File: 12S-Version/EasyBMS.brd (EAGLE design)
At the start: 49 x 100 mm, 145 parts, among them IC1 LTC6811IG-2#PBF, Q10 BSS84LT1G, Q11 BSS84LT1G, Q12 BSS84LT1G, Q13 BSS84LT1G, Q2 BSS84LT1G, Q3 BSS84LT1G, Q4 BSS84LT1G, Q5 BSS84LT1G, Q6 BSS84LT1G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

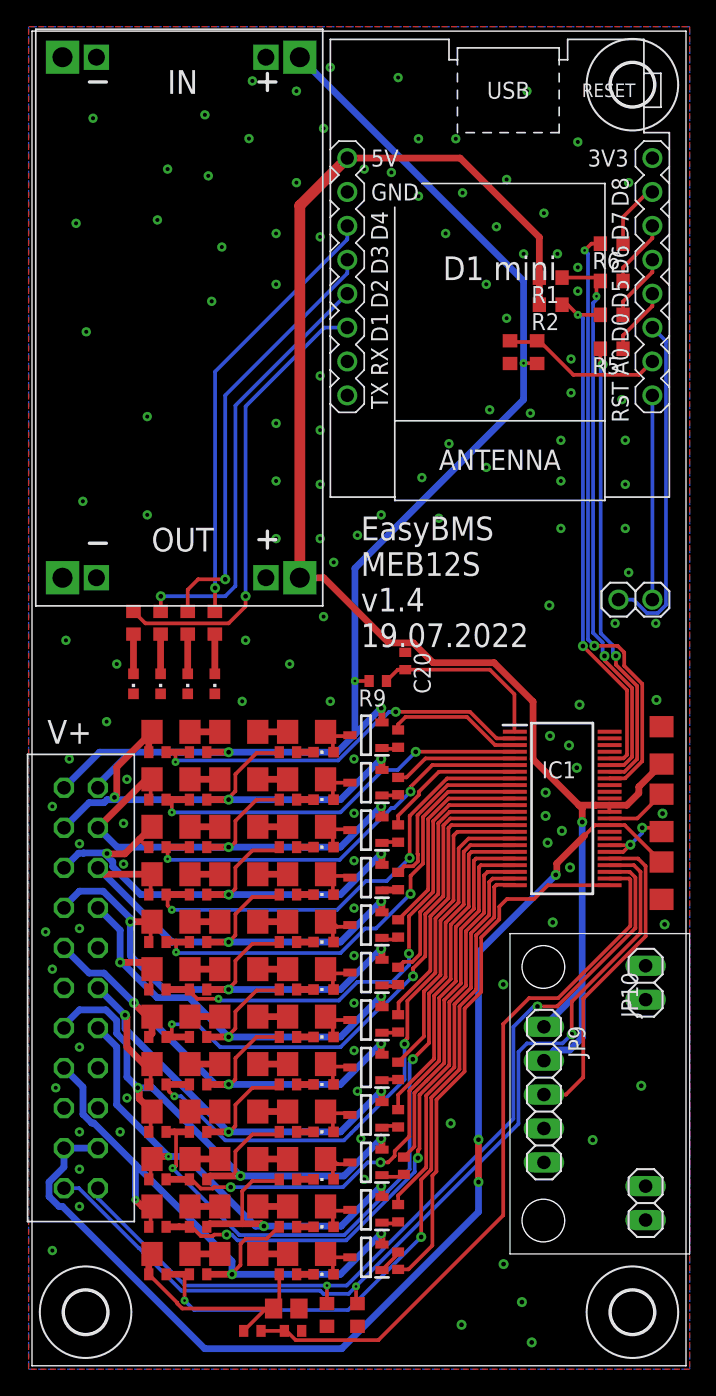
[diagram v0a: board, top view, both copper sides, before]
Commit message: Bugfix of SPI MISO pullup and Bat C1- connection
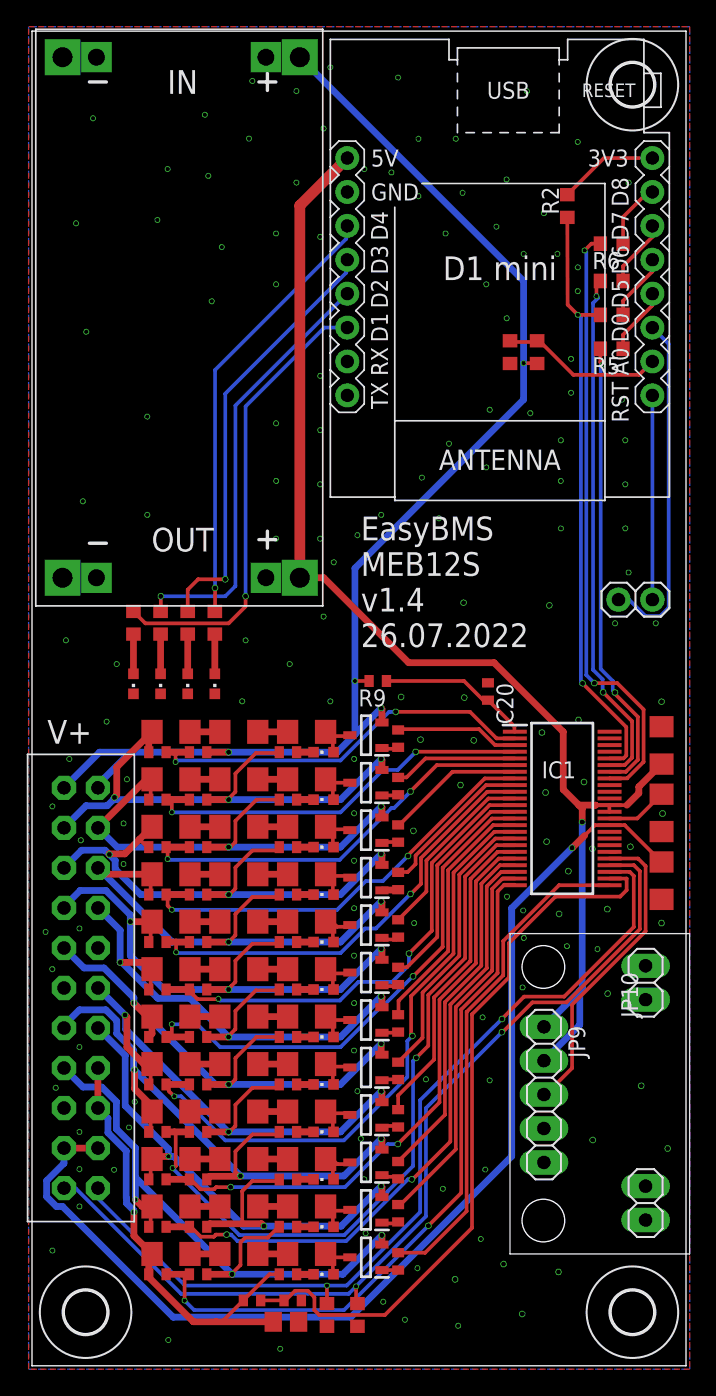
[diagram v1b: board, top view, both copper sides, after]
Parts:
- removed R1: 5K1, rcl:R0603
- moved R2 7.50 mm to (40.1, 86.9), turned to 90 degrees
- moved C20 6.61 mm to (34.2, 50.5)
- moved C5 2.29 mm to (19.5, 4.90)
- moved R3 2.29 mm to (16.5, 4.90)
- moved R13 0.99 mm to (19.0, 3.30)
- moved R34 0.54 mm to (27.4, 14.7)
- moved R10 0.05 mm to (27.4, 7.82), turned to 270 degrees
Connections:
- removed net 3V3: U$2.JP1.8
- new net +3V3: R2.2, U$2.JP1.8
- net 5VDC: no longer R1.2, R2.2
- net C1-: now also JP7.15_TOTAL-, JP7.17_TOTAL-
- net GND: no longer JP7.15_TOTAL-, JP7.17_TOTAL-
- net MOSI: no longer R1.1
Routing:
- net 5VDC: track 122.5 -> 97.4 mm
- net C1-: track 17.7 -> 34.1 mm, vias 0 -> 1
- net +3V3: track 0.00 -> 7.51 mm
- net MISO: track 39.2 -> 45.2 mm
- net GND: track 6.86 -> 1.24 mm, vias 128 -> 154
- net MOSI: track 42.1 -> 39.2 mm
- net VREF2: track 86.5 -> 83.8 mm, vias 3 -> 1
- net S1: track 39.7 -> 37.5 mm
- net V+: track 13.5 -> 11.4 mm
- net S6: track 20.6 -> 18.8 mm
- net C6: track 41.5 -> 39.7 mm
- net C9: track 34.7 -> 32.9 mm
- net S7: track 18.5 -> 16.7 mm
- net C7: track 38.0 -> 36.2 mm
- net S8: track 15.6 -> 13.9 mm
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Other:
- board text added: "EasyBMS MEB12S v1.4 26.07.2022"
- board text removed: "EasyBMS MEB12S v1.4 19.07.2022"

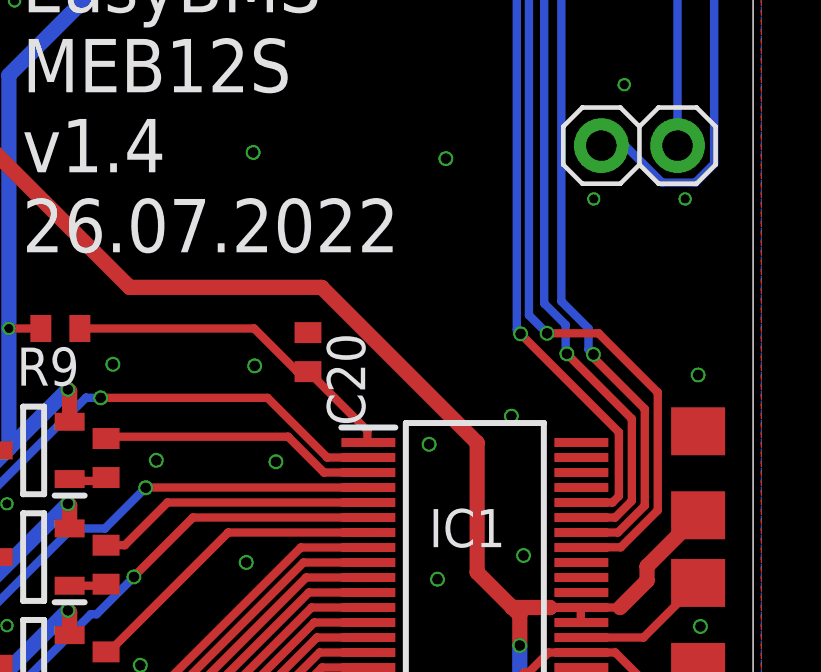
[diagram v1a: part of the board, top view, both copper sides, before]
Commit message: new branch for LTC68xx-1 chip, small changes on base board
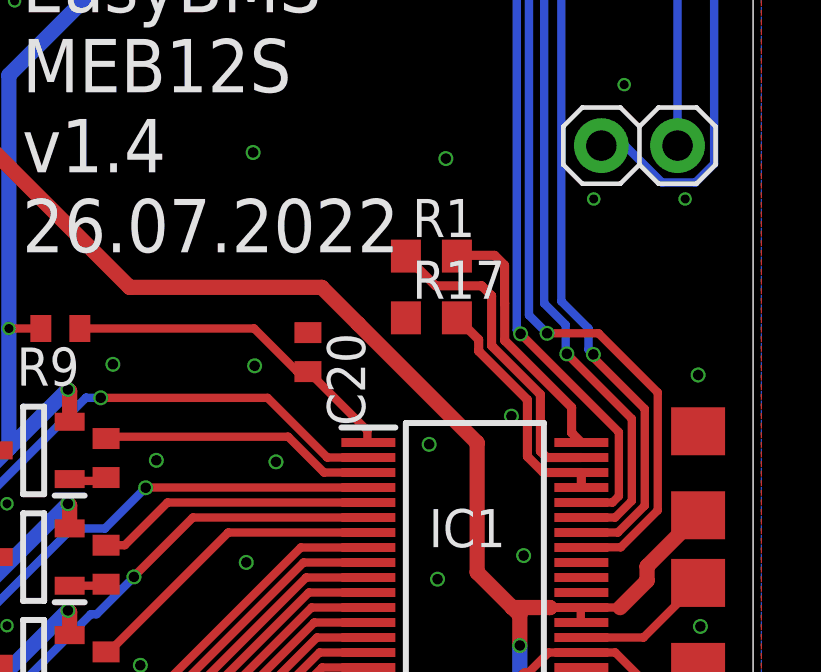
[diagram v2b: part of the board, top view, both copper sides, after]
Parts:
- added R1: 100R, rcl:R0603
- added R17: 20k, rcl:R0603
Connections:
- new net IBIAS: IC1.45, IC1.46, R17.2
- new net IMB: IC1.47, R1.1
- new net IPB: IC1.48, R1.2
- net GND: now also R17.1; no longer IC1.45, IC1.46, IC1.47, IC1.48
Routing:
- net IMB: track 0.00 -> 10.7 mm
- net IPB: track 0.00 -> 8.70 mm
- net IBIAS: track 0.00 -> 8.12 mm
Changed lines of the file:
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@@
 <drawing>
 <settings>
-<setting alwaysvectorfont="yes"/>
+<setting alwaysvectorfont="no"/>
 <setting verticaltext="up"/>
 </settings>
@@
 <attribute name="VALUE" x="18.3896" y="0.762" size="1.27" layer="27"/>
 </element>
+<element name="R1" library="rcl" library_urn="urn:adsk.eagle:library:334" package="R0603" package3d_urn="urn:adsk.eagle:package:23555/2" value="100R" x="38.2778" y="53.721" smashed="yes">
+<attribute name="NAME" x="37.6428" y="54.356" size="1.27" layer="25"/>
+<attribute name="VALUE" x="37.6428" y="51.816" size="1.27" layer="27"/>
+</element>
+<element name="R17" library="rcl" library_urn="urn:adsk.eagle:library:334" package="R0603" package3d_urn="urn:adsk.eagle:package:23555/2" value="20k" x="38.2778" y="51.6636" smashed="yes">
+<attribute name="NAME" x="37.6428" y="52.2986" size="1.27" layer="25"/>
+<attribute name="VALUE" x="37.6428" y="49.7586" size="1.27" layer="27"/>
+</element>
 </elements>
 <signals>
@@
 <wire x1="44.573" y1="42.0076" x2="45.466" y2="42.9006" width="0.2794" layer="1"/>
 <wire x1="28.2194" y1="52.6796" x2="34.6202" y2="52.6796" width="0.508" layer="1"/>
-<wire x1="34.6202" y1="52.6796" x2="39.8018" y2="47.498" width="0.508" layer="1"/>
+<wire x1="34.6202" y1="52.6796" x2="35.8394" y2="51.4604" width="0.508" layer="1"/>
+<wire x1="35.8394" y1="51.4604" x2="39.8018" y2="47.498" width="0.508" layer="1"/>
 <wire x1="21.855" y1="59.044" x2="28.2194" y2="52.6796" width="0.508" layer="1"/>
 <wire x1="39.8018" y1="43.18" x2="39.8018" y2="47.498" width="0.508" layer="1"/>
@@
 <contactref element="IC1" pad="30"/>
 <contactref element="IC1" pad="40"/>
-<contactref element="IC1" pad="48"/>
-<contactref element="IC1" pad="47"/>
-<contactref element="IC1" pad="46"/>
-<contactref element="IC1" pad="45"/>
 <contactref element="C1" pad="2"/>
 <contactref element="C5" pad="2"/>
@@
 <via x="41.9862" y="38.735" extent="1-16" drill="0.35"/>
 <via x="6.1468" y="14.6812" extent="1-16" drill="0.3"/>
+<contactref element="R17" pad="1"/>
 </signal>
 <signal name="N$202">
@@
 <wire x1="42.8502" y1="90.487" x2="46.482" y2="90.487" width="0.2794" layer="1"/>
 </signal>
+<signal name="IPB">
+<contactref element="IC1" pad="48"/>
+<contactref element="R1" pad="2"/>
+<wire x1="43.2756" y1="47.5076" x2="42.9514" y2="47.8318" width="0.3048" layer="1"/>
+<wire x1="40.719" y1="52.1434" x2="40.7162" y2="52.1462" width="0.3048" layer="1"/>
+<wire x1="40.719" y1="50.9104125" x2="40.719" y2="52.1434" width="0.3048" layer="1"/>
+<wire x1="42.9514" y1="48.6780125" x2="40.719" y2="50.9104125" width="0.3048" layer="1"/>
+<wire x1="40.7162" y1="52.1462" x2="40.7162" y2="53.4162" width="0.3048" layer="1"/>
+<wire x1="40.7162" y1="53.4162" x2="40.386" y2="53.7464" width="0.3048" layer="1"/>
+<wire x1="40.386" y1="53.7464" x2="39.1532" y2="53.7464" width="0.3048" layer="1"/>
+<wire x1="39.1532" y1="53.7464" x2="39.1278" y2="53.721" width="0.3048" layer="1"/>
+<wire x1="42.9514" y1="47.8318" x2="42.9514" y2="48.6780125" width="0.3048" layer="1"/>
+</signal>
+<signal name="IMB">
+<contactref element="IC1" pad="47"/>
+<contactref element="R1" pad="1"/>
+<wire x1="37.4278" y1="53.721" x2="38.4184" y2="52.7304" width="0.3048" layer="1"/>
+<wire x1="38.4184" y1="52.7304" x2="39.9542" y2="52.7304" width="0.3048" layer="1"/>
+<wire x1="39.9542" y1="52.7304" x2="40.2844" y2="52.4002" width="0.3048" layer="1"/>
+<wire x1="40.2844" y1="52.4002" x2="40.2844" y2="50.73435" width="0.3048" layer="1"/>
+<wire x1="42.121" y1="47.0076" x2="43.2756" y2="47.0076" width="0.3048" layer="1"/>
+<wire x1="40.2844" y1="50.73435" x2="41.91" y2="49.10875" width="0.3048" layer="1"/>
+<wire x1="41.91" y1="49.10875" x2="41.91" y2="47.2186" width="0.3048" layer="1"/>
+<wire x1="41.91" y1="47.2186" x2="42.121" y2="47.0076" width="0.3048" layer="1"/>
+</signal>
+<signal name="IBIAS">
+<contactref element="IC1" pad="46"/>
+<contactref element="IC1" pad="45"/>
+<contactref element="R17" pad="2"/>
+<wire x1="39.1278" y1="51.6636" x2="39.8526" y2="50.9388" width="0.3048" layer="1"/>
+<wire x1="39.8526" y1="50.9388" x2="39.8526" y2="50.5554875" width="0.3048" layer="1"/>
+<wire x1="39.8526" y1="50.5554875" x2="41.4782" y2="48.9298875" width="0.3048" layer="1"/>
+<wire x1="41.4782" y1="47.0397375" x2="42.0103375" y2="46.5076" width="0.3048" layer="1"/>
+<wire x1="42.0103375" y1="46.5076" x2="43.2756" y2="46.5076" width="0.3048" layer="1"/>
+<wire x1="41.4782" y1="48.9298875" x2="41.4782" y2="47.0397375" width="0.3048" layer="1"/>
+<wire x1="43.2756" y1="46.0076" x2="43.2756" y2="46.5076" width="0.3048" layer="1"/>
+</signal>
 </signals>

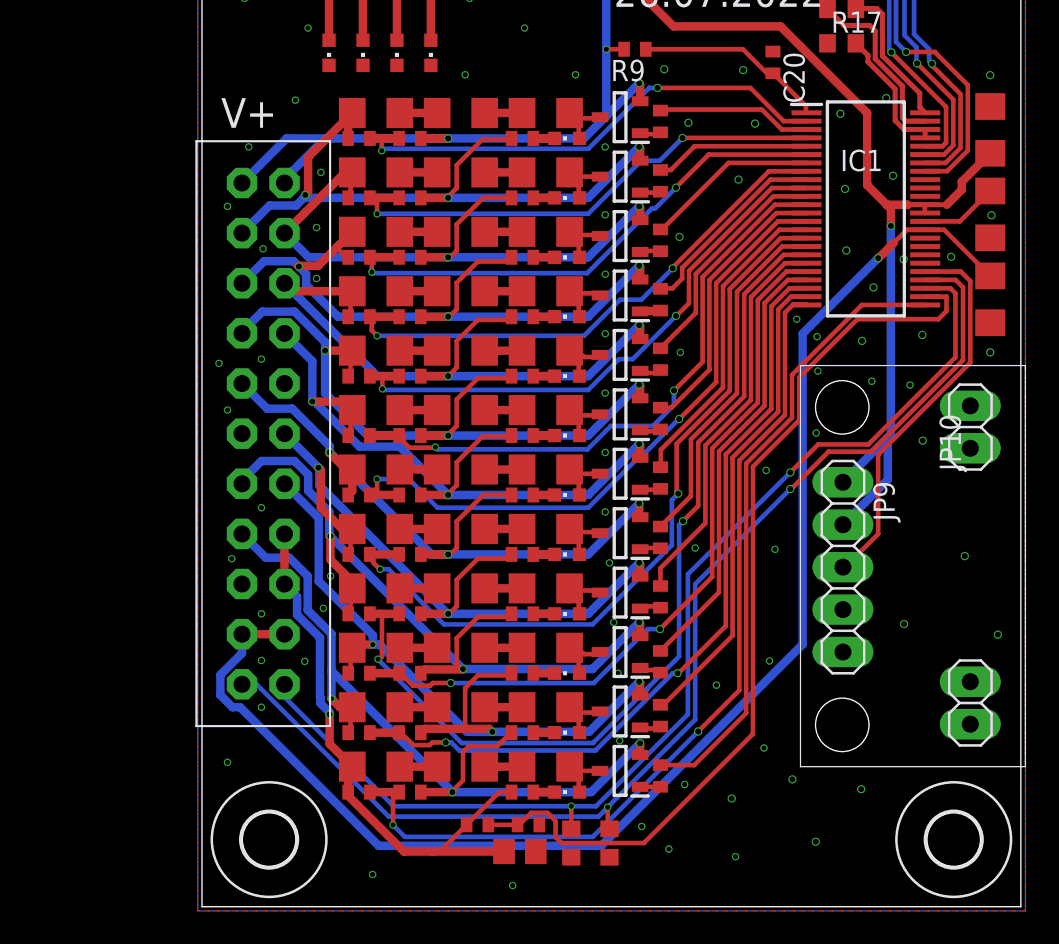
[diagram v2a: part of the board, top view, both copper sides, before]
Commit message: symbol of 6811-1 replaced to a original -1 symbol
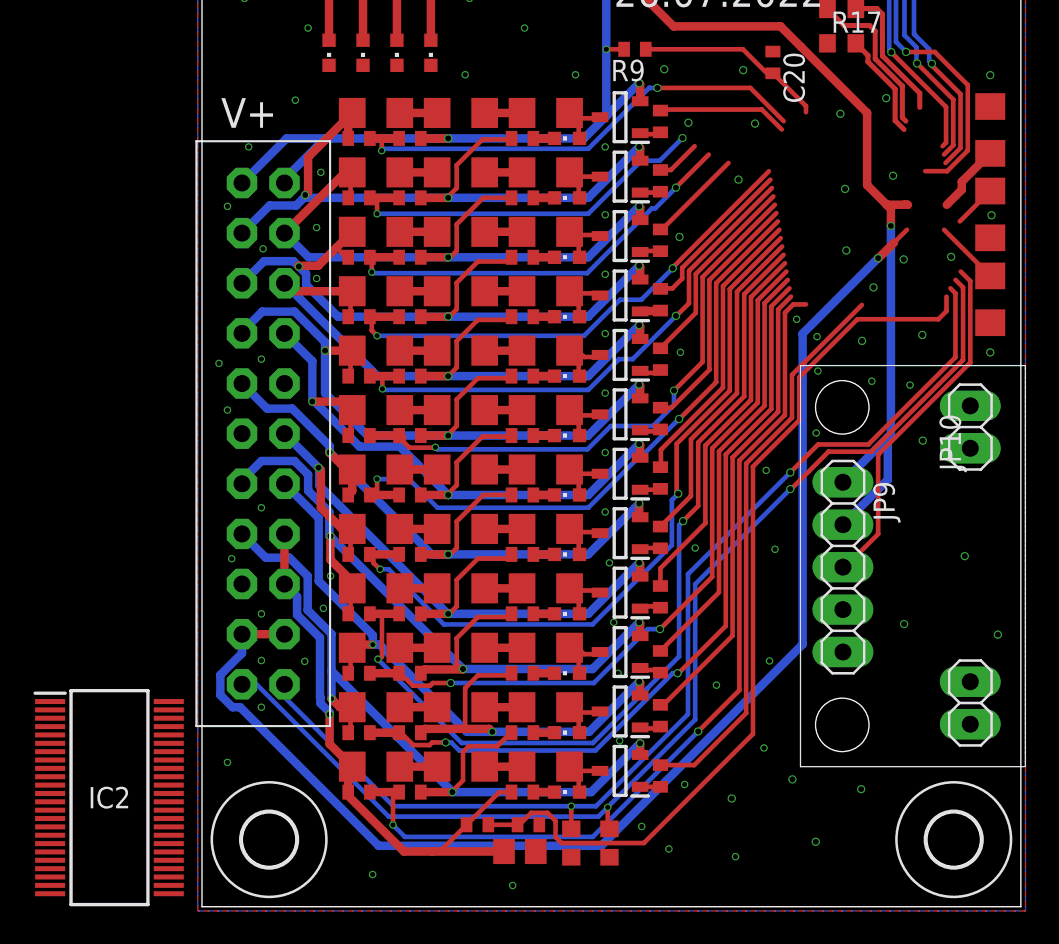
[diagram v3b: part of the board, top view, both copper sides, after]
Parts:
- removed IC1: LTC6811IG-2#PBF, SamacSys_Parts:SOP50P780X200-48N
- added IC2: LTC6811IG-1#PBF, SamacSys_Parts:SOP50P780X200-48N
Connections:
- net 5VDC: now also IC2.36, IC2.37; no longer IC1.36, IC1.37
- net C0: now also IC2.26; no longer IC1.26
- net C1: now also IC2.24; no longer IC1.24
- net C10: now also IC2.6; no longer IC1.6
- net C11: now also IC2.4; no longer IC1.4
- net C12: now also IC2.2; no longer IC1.2
- net C2: now also IC2.22; no longer IC1.22
- net C3: now also IC2.20; no longer IC1.20
- net C4: now also IC2.18; no longer IC1.18
- net C5: now also IC2.16; no longer IC1.16
- net C6: now also IC2.14; no longer IC1.14
- net C7: now also IC2.12; no longer IC1.12
- net C8: now also IC2.10; no longer IC1.10
- net C9: now also IC2.8; no longer IC1.8
- net CSB: now also IC2.41; no longer IC1.41
- net GND: now also IC2.30, IC2.31, IC2.40; no longer IC1.30, IC1.31, IC1.40
- net GPIO4: now also IC2.32; no longer IC1.32
- net GPIO5: now also IC2.33; no longer IC1.33
- net IBIAS: now also IC2.45, IC2.46; no longer IC1.45, IC1.46
- net IMB: now also IC2.47; no longer IC1.47
- net IPB: now also IC2.48; no longer IC1.48
- net ISIGNAL: now also IC2.29; no longer IC1.29
- net MISO: now also IC2.44; no longer IC1.44
- net MOSI: now also IC2.43; no longer IC1.43
- net S1: now also IC2.25; no longer IC1.25
- net S10: now also IC2.7; no longer IC1.7
- net S11: now also IC2.5; no longer IC1.5
- net S12: now also IC2.3; no longer IC1.3
- net S2: now also IC2.23; no longer IC1.23
- net S3: now also IC2.21; no longer IC1.21
- net S4: now also IC2.19; no longer IC1.19
- net S5: now also IC2.17; no longer IC1.17
- net S6: now also IC2.15; no longer IC1.15
- net S7: now also IC2.13; no longer IC1.13
- net S8: now also IC2.11; no longer IC1.11
- net S9: now also IC2.9; no longer IC1.9
- net SCK: now also IC2.42; no longer IC1.42
- net V+: now also IC2.1; no longer IC1.1
- net VREF1: now also IC2.35; no longer IC1.35
- net VREF2: now also IC2.34; no longer IC1.34
- net VTEMP1: now also IC2.27; no longer IC1.27
- net VTEMP2: now also IC2.28; no longer IC1.28
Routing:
- net C11: track 30.3 -> 22.9 mm
- net S11: track 9.33 -> 2.64 mm
- net C10: track 31.7 -> 25.8 mm
- net S10: track 10.4 -> 5.72 mm
- net S1: track 37.5 -> 33.7 mm
- net 5VDC: track 97.4 -> 94.3 mm
- net C9: track 32.9 -> 30.6 mm
- net VREF2: track 83.8 -> 81.6 mm
- net S9: track 11.8 -> 9.66 mm
- net ISIGNAL: track 23.3 -> 21.2 mm
- net C8: track 34.1 -> 32.0 mm
- net VREF1: track 4.65 -> 2.57 mm
- net S8: track 13.9 -> 11.9 mm
- net C7: track 36.2 -> 34.3 mm
- net VTEMP2: track 70.6 -> 68.8 mm
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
